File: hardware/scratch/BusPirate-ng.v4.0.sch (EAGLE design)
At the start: 133 parts, among them CON1 CON-USB-F-MICRO-B, IC10 74LVC1G07DBV, IC11 IC_BUFF_SN74LVC1T45DBV, IC12 74LVC1G07DBV, IC13 IC_BUFF_SN74LVC1T45DBV, IC14 74LVC1G07DBV, IC15 IC_BUFF_SN74LVC1T45DBV, IC16 74LVC1G07DBV, IC17 IC_BUFF_SN74LVC1T45DBV, IC2 IC_MEM_23LC1024, IC3 IC_MEM_23LC1024, IC4 IC_74AC573, IC5 IC_BL1551, IC6 IC_BL1551, IC7 74HCT4066PW, IC8 74LVC1G07DBV, IC9 IC_BUFF_SN74LVC1T45DBV, J1 CON_HEADER_1X04, J2 CON_HEADER_1X03-PTH, J3 CON_HEADER_2X02-PTH, J5 CON_HEADER_1X10-RIGHT_ANGLED_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, U1 IC_FPGA_ICE40HX4K, U2 IC_UC_STM32F103ZX, U3 IC_MEM_AT45DB041D

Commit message: connect remaining loose nets, finished routing -connect VCC of 74LVCT45 to pull-up voltage VPUN -connect pull-up resistors of FPGA_CRESET and FPGA_CDONE to to 3V3
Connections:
- removed net VCC: R38.2, R39.2
- removed net VCCEXT: C10.2, C2.2, C4.2, C6.2, C8.2, IC11.VCCB, IC13.VCCB, IC15.VCCB, IC17.VCCB, IC9.VCCB
- net 3V3: now also R38.2, R39.2
- net USBLED: no longer U2U.UART4_TX/USART3_TX('01')/FT/PC10
- net VPUN: now also C10.2, C2.2, C4.2, C6.2, C8.2, IC11.VCCB, IC13.VCCB, IC15.VCCB, IC17.VCCB, IC9.VCCB
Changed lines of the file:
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@@
 <attribute name="VALUE" x="76.2" y="375.92" size="1.778" layer="96"/>
 </instance>
-<instance part="P+1" gate="VCC" x="83.82" y="388.62"/>
-<instance part="P+3" gate="VCC" x="81.28" y="386.08"/>
+<instance part="P+1" gate="VCC" x="83.82" y="388.62" smashed="yes"/>
+<instance part="P+3" gate="VCC" x="81.28" y="388.62" smashed="yes"/>
 <instance part="C21" gate="G$1" x="-195.58" y="543.56" smashed="yes" rot="R180">
 <attribute name="NAME" x="-195.58" y="548.64" size="1.778" layer="95" rot="R90"/>
@@
 <junction x="144.78" y="284.48"/>
 </segment>
+<segment>
+<pinref part="R38" gate="G$1" pin="2"/>
+<pinref part="P+1" gate="VCC" pin="VCC"/>
+<wire x1="83.82" y1="386.08" x2="83.82" y2="383.54" width="0.1524" layer="91"/>
+<label x="83.82" y="388.62" size="1.778" layer="95"/>
+</segment>
+<segment>
+<pinref part="R39" gate="G$1" pin="2"/>
+<pinref part="P+3" gate="VCC" pin="VCC"/>
+<wire x1="81.28" y1="381" x2="81.28" y2="386.08" width="0.1524" layer="91"/>
+<label x="81.28" y="388.62" size="1.778" layer="95" align="bottom-right"/>
+</segment>
 </net>
 <net name="N$7" class="0">
@@
 <wire x1="-248.92" y1="139.7" x2="-251.46" y2="139.7" width="0.1524" layer="91"/>
 <label x="-251.46" y="139.7" size="1.778" layer="95" align="center-right"/>
-</segment>
-<segment>
-<pinref part="U2" gate="U" pin="UART4_TX/USART3_TX('01')/FT/PC10"/>
-<wire x1="-142.24" y1="121.92" x2="-139.7" y2="121.92" width="0.1524" layer="91"/>
 </segment>
 </net>
@@
 <pinref part="RN1" gate="C" pin="1"/>
 </segment>
+<segment>
+<pinref part="IC17" gate="G$1" pin="VCCB"/>
+<wire x1="175.26" y1="281.94" x2="175.26" y2="284.48" width="0.1524" layer="91"/>
+<label x="175.26" y="287.02" size="1.778" layer="95" align="center-right"/>
+<pinref part="C10" gate="G$1" pin="2"/>
+<wire x1="175.26" y1="284.48" x2="175.26" y2="287.02" width="0.1524" layer="91"/>
+<junction x="175.26" y="284.48"/>
+</segment>
+<segment>
+<pinref part="IC15" gate="G$1" pin="VCCB"/>
+<wire x1="179.07" y1="335.28" x2="179.07" y2="339.09" width="0.1524" layer="91"/>
+<label x="177.8" y="340.36" size="1.778" layer="95" align="center-right"/>
+<pinref part="C8" gate="G$1" pin="2"/>
+<wire x1="179.07" y1="339.09" x2="179.07" y2="341.63" width="0.1524" layer="91"/>
+<junction x="179.07" y="339.09"/>
+</segment>
+<segment>
+<pinref part="IC13" gate="G$1" pin="VCCB"/>
+<wire x1="175.26" y1="386.08" x2="175.26" y2="388.62" width="0.1524" layer="91"/>
+<label x="175.26" y="391.16" size="1.778" layer="95" align="center-right"/>
+<pinref part="C6" gate="G$1" pin="2"/>
+<wire x1="175.26" y1="388.62" x2="175.26" y2="391.16" width="0.1524" layer="91"/>
+<junction x="175.26" y="388.62"/>
+</segment>
+<segment>
+<pinref part="IC11" gate="G$1" pin="VCCB"/>
+<wire x1="175.26" y1="436.88" x2="175.26" y2="439.42" width="0.1524" layer="91"/>
+<label x="175.26" y="441.96" size="1.778" layer="95" align="center-right"/>
+<pinref part="C4" gate="G$1" pin="2"/>
+<wire x1="175.26" y1="439.42" x2="175.26" y2="441.96" width="0.1524" layer="91"/>
+<junction x="175.26" y="439.42"/>
+</segment>
+<segment>
+<pinref part="IC9" gate="G$1" pin="VCCB"/>
+<wire x1="175.26" y1="497.84" x2="175.26" y2="500.38" width="0.1524" layer="91"/>
+<label x="175.26" y="502.92" size="1.778" layer="95" align="center-right"/>
+<pinref part="C2" gate="G$1" pin="2"/>
+<wire x1="175.26" y1="500.38" x2="175.26" y2="502.92" width="0.1524" layer="91"/>
+<junction x="175.26" y="500.38"/>
+</segment>
 </net>
 <net name="UART_RX" class="0">
@@
 </segment>
 </net>
-<net name="VCC" class="0">
-<segment>
-<pinref part="R38" gate="G$1" pin="2"/>
-<pinref part="P+1" gate="VCC" pin="VCC"/>
-<wire x1="83.82" y1="386.08" x2="83.82" y2="383.54" width="0.1524" layer="91"/>
-</segment>
-<segment>
-<pinref part="R39" gate="G$1" pin="2"/>
-<pinref part="P+3" gate="VCC" pin="VCC"/>
-<wire x1="81.28" y1="381" x2="81.28" y2="383.54" width="0.1524" layer="91"/>
-</segment>
-</net>
-<net name="VCCEXT" class="0">
-<segment>
-<pinref part="IC9" gate="G$1" pin="VCCB"/>
-<wire x1="175.26" y1="497.84" x2="175.26" y2="500.38" width="0.1524" layer="91"/>
-<label x="175.26" y="502.92" size="1.778" layer="95" align="center-right"/>
-<pinref part="C2" gate="G$1" pin="2"/>
-<wire x1="175.26" y1="500.38" x2="175.26" y2="502.92" width="0.1524" layer="91"/>
-<junction x="175.26" y="500.38"/>
-</segment>
-<segment>
-<pinref part="IC11" gate="G$1" pin="VCCB"/>
-<wire x1="175.26" y1="436.88" x2="175.26" y2="439.42" width="0.1524" layer="91"/>
-<label x="175.26" y="441.96" size="1.778" layer="95" align="center-right"/>
-<pinref part="C4" gate="G$1" pin="2"/>
-<wire x1="175.26" y1="439.42" x2="175.26" y2="441.96" width="0.1524" layer="91"/>
-<junction x="175.26" y="439.42"/>
-</segment>
-<segment>
-<pinref part="IC13" gate="G$1" pin="VCCB"/>
-<wire x1="175.26" y1="386.08" x2="175.26" y2="388.62" width="0.1524" layer="91"/>
-<label x="175.26" y="391.16" size="1.778" layer="95" align="center-right"/>
-<pinref part="C6" gate="G$1" pin="2"/>
-<wire x1="175.26" y1="388.62" x2="175.26" y2="391.16" width="0.1524" layer="91"/>
-<junction x="175.26" y="388.62"/>
-</segment>
-<segment>
-<pinref part="IC15" gate="G$1" pin="VCCB"/>
-<wire x1="179.07" y1="335.28" x2="179.07" y2="339.09" width="0.1524" layer="91"/>
-<label x="177.8" y="340.36" size="1.778" layer="95" align="center-right"/>
-<pinref part="C8" gate="G$1" pin="2"/>
-<wire x1="179.07" y1="339.09" x2="179.07" y2="341.63" width="0.1524" layer="91"/>
-<junction x="179.07" y="339.09"/>
-</segment>
-<segment>
-<pinref part="IC17" gate="G$1" pin="VCCB"/>
-<wire x1="175.26" y1="281.94" x2="175.26" y2="284.48" width="0.1524" layer="91"/>
-<label x="175.26" y="287.02" size="1.778" layer="95" align="center-right"/>
-<pinref part="C10" gate="G$1" pin="2"/>
-<wire x1="175.26" y1="284.48" x2="175.26" y2="287.02" width="0.1524" layer="91"/>
-<junction x="175.26" y="284.48"/>
-</segment>
-</net>

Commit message: renumber parts
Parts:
- removed C55: 0.1uF, rcl:C-EUC0603
- removed IC17: IC_BUFF_SN74LVC1T45DBV, dp_devices.v6:IC_BUFF_SN74LVC1T45DBV
- removed R34, R35: 100K, rcl:R-EU_R0603
- removed R36: 1M, rcl:R-EU_R0603
- removed R37, R40: 10K, dp_devices:RESISTOR-0603
- removed R38: 10K, rcl:R-EU_R0603
- added C28: 0.1uF, rcl:C-EUC0603
- added IC1: IC_MEM_23LC1024, dp_devices:IC_MEM_23LC1024
- added R1: 1.5K, dp_devices.v6:RESISTOR-0603
- added R10, R11, R12, R9: 10K, resistor:R-EU_R0603
- added R21: 100K, rcl:R-EU_R0603
- C1: value 0.1uF -> 10uF; device rcl:C-EUC0603 -> rcl:CPOL-EUSMCA
- C10, C27: device rcl:C-EUC0603 -> dp_devices.v6:CAPACITOR_NPOL-0402
- C11: value 10uF -> 0.1uF; device rcl:CPOL-EUSMCA -> rcl:C-EUC0603
- C12, C32: value 1uf -> 0.1uF
- C13: value 1uF -> 0.1uF
- C16: value 1uF -> 22pF
- C17: value 0.1uF -> 1uF; device rcl:C-EUC0603 -> rcl:CPOL-EUSMCA
- C18: value 0.1uF -> 22pF
- C36: value 22pF -> 1uf
- C37: value 22pF -> 1uF
- C38: value 0.1uF -> 1uf
- C44: value 0.1uF -> 1uF
- C45, C47: device dp_devices.v6:CAPACITOR_NPOL-0402 -> rcl:C-EUC0603
- C53: value 1uF -> 0.1uF; device rcl:CPOL-EUSMCA -> rcl:C-EUC0603
- IC10, IC8: value 74LVC1G07DBV -> IC_BUFF_SN74LVC1T45DBV; device 74xx-little-de:74LVC1G07DBV -> dp_devices.v6:IC_BUFF_SN74LVC1T45DBV
- IC14: value 74LVC1G07DBV -> IC_BL1551; device 74xx-little-de:74LVC1G07DBV -> dp_devices.v6:IC_BL1551
- IC15: value IC_BUFF_SN74LVC1T45DBV -> IC_BL1551; device dp_devices.v6:IC_BUFF_SN74LVC1T45DBV -> dp_devices.v6:IC_BL1551
- IC16: value 74LVC1G07DBV -> 74HCT4066PW; device 74xx-little-de:74LVC1G07DBV -> 40xx:4066TS
- IC3: value IC_MEM_23LC1024 -> IC_74AC573; device dp_devices:IC_MEM_23LC1024 -> dp_devices:IC_74AC573-TSSOP-20
- IC4: value IC_74AC573 -> 74LVC1G07DBV; device dp_devices:IC_74AC573-TSSOP-20 -> 74xx-little-de:74LVC1G07DBV
- IC5, IC6: value IC_BL1551 -> 74LVC1G07DBV; device dp_devices.v6:IC_BL1551 -> 74xx-little-de:74LVC1G07DBV
- IC7: value 74HCT4066PW -> 74LVC1G07DBV; device 40xx:4066TS -> 74xx-little-de:74LVC1G07DBV
- J1: value CON_HEADER_1X04 -> CON_HEADER_2X02-PTH; device dp_devices.v6:CON_HEADER_1X04 -> dp_devices:CON_HEADER_2X02-PTH
- J2: value CON_HEADER_1X03-PTH -> CON_HEADER_1X04; device dp_devices.v6:CON_HEADER_1X03-PTH -> dp_devices.v6:CON_HEADER_1X04
- J3: value CON_HEADER_2X02-PTH -> CON_HEADER_1X03-PTH; device dp_devices:CON_HEADER_2X02-PTH -> dp_devices.v6:CON_HEADER_1X03-PTH
- R13, R14: value 10K -> 1K1; device resistor:R-EU_R0603 -> dp_devices:RESISTOR-0603
- R16: value 1K1 -> 10K; device dp_devices:RESISTOR-0603 -> rcl:R-EU_R0603
- R18: value 10K -> 1K1; device dp_devices.v6:RESISTOR-0603 -> dp_devices:RESISTOR-0603
- R19, R20: value 1K1 -> 100K; device dp_devices:RESISTOR-0603 -> rcl:R-EU_R0603
- R2: value 1.5K -> 22R
- R25, R26, R31: value 100K -> 1M
- R3: value 10K -> 22R; device rcl:R-EU_R0603 -> dp_devices.v6:RESISTOR-0603
- R30, R33: value 1M -> 100K
- R4: device rcl:R-EU_R0603 -> dp_devices:RESISTOR-0603
- R5: value 22R -> 10K
- R6: value 22R -> 10K; device dp_devices.v6:RESISTOR-0603 -> dp_devices:RESISTOR-0603
- R7, R8: device resistor:R-EU_R0603 -> rcl:R-EU_R0603
- U1: value IC_FPGA_ICE40HX4K -> IC_MEM_AT45DB041D; device dp_devices.v6:IC_FPGA_ICE40HX4K -> dp_devices.v6:IC_MEM_AT45DB041D
- U3: value IC_MEM_AT45DB041D -> IC_FPGA_ICE40HX4K; device dp_devices.v6:IC_MEM_AT45DB041D -> dp_devices.v6:IC_FPGA_ICE40HX4K
- VR3: value MCP1801T-5002I/OT -> MCP1801T-1202I/OT
- VR4: value MCP1801T-1202I/OT -> MCP1801T-5002I/OT
- renumbered J5 to J4, R39 to R15, XTAL2 to XTAL1
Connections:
- net 1V2: now also C23.2, C26.2, C27.1, C31.2, C35.2, C38.1, U3BANK0.VCC@0, U3BANK0.VCCPLL1, U3BANK1.VCC@0, U3BANK2.VCC@0, U3BANK2.VCCPLL0, U3BANK3.VCC@0, VR3.OUT; no longer C20.1, C32.1, C38.2, C41.2, C48.2, C55.2, U1BANK0.VCC@0, U1BANK0.VCCPLL1, U1BANK1.VCC@0, U1BANK2.VCC@0, U1BANK2.VCCPLL0, U1BANK3.VCC@0, VR4.OUT
- net 3V3: now also C10.1, C11.2, C12.2, C13.2, C15.2, C17.+, C19.2, C2.2, C20.1, C28.2, C3.2, C32.2, C36.1, C39.1, C4.2, C40.1, C41.1, C42.1, C43.1, C5.2, C50.1, C52.1, C54.1, C6.2, C7.2, C8.2, C9.2, IC10.VCCA, IC1SUP.V+, IC3IC.LE, IC3PWR.V+, IC4P.VCC, IC5P.VCC, IC6P.VCC, IC7P.VCC, IC8.VCCA, J1.2, J1.4, J2.1, R13.2, R19.2, R20.2, R21.2, R23.2, R5.2, U1.!RST, U1.!WP, U1.VCC, U3BANK0.VCCIO_0@0, U3BANK0.VCCIO_0@1, U3BANK1.VCCIO_1@0, U3BANK1.VCCIO_1@1, U3BANK1.VPP_2V5, U3BANK2.VCCIO_2@0, U3BANK2.VCCIO_2@1, U3BANK3.VCCIO_3@0, U3BANK3.VCCIO_3@1, U3SPI.VCC_SPI; no longer C1.1, C12.1, C14.1, C15.1, C17.1, C23.2, C26.2, C27.2, C3.1, C31.2, C35.2, C39.2, C40.2, C42.2, C43.2, C44.2, C45.1, C46.2, C47.1, C49.2, C5.1, C50.2, C52.2, C53.+, C54.2, C7.1, C9.1, IC10P.VCC, IC14P.VCC, IC15.VCCA, IC16P.VCC, IC17.VCCA, IC3SUP.V+, IC4IC.LE, IC4PWR.V+, IC8P.VCC, J1.1, J3.2, J3.4, R18.2, R25.2, R28.2, R31.2, R34.2, R38.2, U1BANK0.VCCIO_0@0, U1BANK0.VCCIO_0@1, U1BANK1.VCCIO_1@0, U1BANK1.VCCIO_1@1, U1BANK1.VPP_2V5, U1BANK2.VCCIO_2@0, U1BANK2.VCCIO_2@1, U1BANK3.VCCIO_3@0, U1BANK3.VCCIO_3@1, U1SPI.VCC_SPI, U3.!RST, U3.!WP, U3.VCC
- net ADC1: now also R10.2, R9.2; no longer R7.2, R8.2
- net ADC2: now also RN2A.2, RN2B.2; no longer RN1A.2, RN1B.2
- net ADC3: now also RN1C.2, RN1D.2; no longer RN2C.2, RN2D.2
- net ADC4: now also RN1A.2, RN1B.2; no longer RN2A.2, RN2B.2
- net ADC5: now also R11.2, R12.2; no longer R13.2, R14.2
- net ADC6: now also RN2C.2, RN2D.2; no longer RN1C.2, RN1D.2
- net BOOT0: now also J1.1, R8.1; no longer J3.1, R4.1
- net BOOT1: now also J1.3, R7.1; no longer J3.3, R3.1
- net BPIO_AUX: now also IC11.B, IC3IC.6D, IC7A.O, R27.2; no longer IC16A.O, IC17.B, IC4IC.6D, R36.2
- net BPIO_CLOCK: now also IC3IC.3D, IC5A.O, IC9.B, R25.2; no longer IC10A.O, IC11.B, IC4IC.3D, R27.2
- net BPIO_CS: now also IC12A.O, IC13.B, IC3IC.5D, R31.2; no longer IC14A.O, IC15.B, IC4IC.5D, R33.2
- net BPIO_MISO: now also IC10.B, IC3IC.4D, IC6A.O, R26.2; no longer IC12A.O, IC13.B, IC4IC.4D, R30.2
- net BPIO_MOSI: now also IC3IC.2D, IC4A.O, IC8.B; no longer IC4IC.2D, IC8A.O, IC9.B
- net BUFDIR_AUX: now also IC11.DIR, R32.2, U3BANK1.IOR_164; no longer IC17.DIR, R35.2, U1BANK1.IOR_164
- net BUFDIR_CLOCK: now also IC9.DIR, R29.2, U3BANK1.IOR_111; no longer IC11.DIR, R26.2, U1BANK1.IOR_111
- net BUFDIR_CS: now also IC13.DIR, R33.2, U3BANK1.IOR_167; no longer IC15.DIR, R32.2, U1BANK1.IOR_167
- net BUFDIR_MISO: now also IC10.DIR, R30.2, U3BANK1.IOR_118; no longer IC13.DIR, R29.2, U1BANK1.IOR_118
- net BUFDIR_MOSI: now also IC8.DIR, R28.2, U3BANK1.IOR_115; no longer IC9.DIR, R23.2, U1BANK1.IOR_115
- net BUFIO_AUX: now also IC11.A, U3BANK1.IOR_161; no longer IC17.A, U1BANK1.IOR_161
- net BUFIO_CLOCK: now also IC9.A, U3BANK1.IOR_110; no longer IC11.A, U1BANK1.IOR_110
- net BUFIO_CS: now also IC13.A, U3BANK1.IOR_166; no longer IC15.A, U1BANK1.IOR_166
- net BUFIO_MISO: now also IC10.A, U3BANK1.IOR_117; no longer IC13.A, U1BANK1.IOR_117
- net BUFIO_MOSI: now also IC8.A, U3BANK1.IOR_114; no longer IC9.A, U1BANK1.IOR_114
- net BUFOD_AUX: now also IC7A.I, R22.1, U3BANK1.IOR_160; no longer IC16A.I, R34.1, U1BANK1.IOR_160
- net BUFOD_CLOCK: now also IC5A.I, R20.1, U3BANK1.IOR_109; no longer IC10A.I, R25.1, U1BANK1.IOR_109
- net BUFOD_CS: now also IC12A.I, R23.1, U3BANK1.IOR_165; no longer IC14A.I, R31.1, U1BANK1.IOR_165
- net BUFOD_MISO: now also IC6A.I, R21.1, U3BANK1.IOR_116; no longer IC12A.I, R28.1, U1BANK1.IOR_116
- net BUFOD_MOSI: now also IC4A.I, R19.1, U3BANK1.IOR_112; no longer IC8A.I, R22.1, U1BANK1.IOR_112
- net D+: now also R1.1, R3.2; no longer R2.1, R6.2
- net D-: now also R2.2; no longer R5.2
- net FLASH_MISO: now also U1.SO; no longer U3.SO
- net FLASH_MOSI: now also U1.SI; no longer U3.SI
- net FLASH_SCK: now also U1.SCK; no longer U3.SCK
- net FPGA_CDONE: now also U3BANK2.CDONE; no longer U1BANK2.CDONE
- net FPGA_CRESET: now also R16.1, U3BANK2.CRESET_B; no longer R38.1, U1BANK2.CRESET_B
- net FPGA_PROG_CLOCK: now also U3SPI.IOB_107/SCK; no longer U1SPI.IOB_107/SCK
- net FPGA_PROG_CS: now also R6.1, U3SPI.IOB_108/SS; no longer R37.1, U1SPI.IOB_108/SS
- net FPGA_PROG_MISO: now also U3SPI.IOB_105/SDO; no longer U1SPI.IOB_105/SDO
- net FPGA_PROG_MOSI: now also U3SPI.IOB_106/SDI; no longer U1SPI.IOB_106/SDI
- net FSMC_A0: now also U3BANK3.IOL_3A; no longer U1BANK3.IOL_3A
- net FSMC_A1: now also U3BANK3.IOL_3B; no longer U1BANK3.IOL_3B
- net FSMC_A2: now also U3BANK3.IOL_4A; no longer U1BANK3.IOL_4A
- net FSMC_A3: now also U3BANK3.IOL_4B; no longer U1BANK3.IOL_4B
- net FSMC_A4: now also U3BANK3.IOL_5A; no longer U1BANK3.IOL_5A
- net FSMC_A5: now also U3BANK3.IOL_5B; no longer U1BANK3.IOL_5B
- net FSMC_D0: now also U3BANK3.IOL_17B; no longer U1BANK3.IOL_17B
- net FSMC_D1: now also U3BANK3.IOL_17A; no longer U1BANK3.IOL_17A
- net FSMC_D10: now also U3BANK3.IOL_18B; no longer U1BANK3.IOL_18B
- net FSMC_D11: now also U3BANK3.IOL_23A; no longer U1BANK3.IOL_23A
- net FSMC_D12: now also U3BANK3.IOL_23B; no longer U1BANK3.IOL_23B
- net FSMC_D13: now also U3BANK3.IOL_25A; no longer U1BANK3.IOL_25A
- net FSMC_D14: now also U3BANK3.IOL_24B; no longer U1BANK3.IOL_24B
- net FSMC_D15: now also U3BANK3.IOL_24A; no longer U1BANK3.IOL_24A
- net FSMC_D2: now also U3BANK3.IOL_2A; no longer U1BANK3.IOL_2A
- net FSMC_D3: now also U3BANK3.IOL_2B; no longer U1BANK3.IOL_2B
- net FSMC_D4: now also U3BANK3.IOL_10A; no longer U1BANK3.IOL_10A
- net FSMC_D5: now also U3BANK3.IOL_10B; no longer U1BANK3.IOL_10B
- net FSMC_D6: now also U3BANK3.IOL_12A; no longer U1BANK3.IOL_12A
- net FSMC_D7: now also U3BANK3.IOL_12B; no longer U1BANK3.IOL_12B
- net FSMC_D8: now also U3BANK3.IOL_13A; no longer U1BANK3.IOL_13A
- net FSMC_D9: now also U3BANK3.IOL_18A; no longer U1BANK3.IOL_18A
- net FSMC_NE3_CE: now also U3BANK3.IOL_14B; no longer U1BANK3.IOL_14B
- net FSMC_NOE_OE: now also U3BANK3.IOL_8A; no longer U1BANK3.IOL_8A
- net FSMC_NWE_WE: now also U3BANK3.IOL_8B; no longer U1BANK3.IOL_8B
- net GND: now also C1.-, C10.2, C11.1, C12.1, C13.1, C14.1, C15.1, C16.1, C17.-, C18.1, C19.1, C27.2, C28.1, C3.1, C32.1, C36.2, C37.2, C38.2, C39.2, C40.2, C41.2, C42.2, C43.2, C44.2, C45.1, C47.1, C5.1, C50.2, C51.2, C52.2, C53.2, C54.2, C7.1, C9.1, IC10.GND, IC14.GND, IC16P.VSS, IC1SUP.GND, IC3IC.1D, IC3PWR.GND, IC4P.GND, IC5P.GND, IC6P.GND, IC7P.GND, IC8.GND, J2.2, J3.1, R10.1, R12.1, R25.1, R28.1, R31.1, R6.2, R7.2, R8.2, U1.!CS, U1.GND, U3BANK0.GND@0, U3BANK0.GND@1, U3BANK0.GNDPLL1, U3BANK1.GND@0, U3BANK1.GND@1, U3BANK2.GND@0, U3BANK2.GNDPLL0, U3BANK3.GND@0, U3BANK3.GND@1, U3BANK3.GND@2, U3SPI.GND@0; no longer C1.2, C10.1, C11.-, C12.2, C13.2, C14.2, C15.2, C16.2, C17.2, C18.2, C19.2, C27.1, C3.2, C32.2, C36.1, C37.1, C38.1, C39.1, C40.1, C41.1, C42.1, C43.1, C44.1, C45.2, C47.2, C5.2, C50.1, C51.1, C52.1, C53.-, C54.1, C55.1, C7.2, C9.2, IC10P.GND, IC14P.GND, IC16P.GND, IC17.GND, IC3SUP.GND, IC4IC.1D, IC4PWR.GND, IC5.GND, IC6.GND, IC7P.VSS, IC8P.GND, J1.2, J2.1, R14.1, R23.1, R3.2, R35.1, R36.1, R37.2, R40.2, R8.1, U1BANK0.GND@0, U1BANK0.GND@1, U1BANK0.GNDPLL1, U1BANK1.GND@0, U1BANK1.GND@1, U1BANK2.GND@0, U1BANK2.GNDPLL0, U1BANK3.GND@0, U1BANK3.GND@1, U1BANK3.GND@2, U1SPI.GND@0, U3.!CS, U3.GND
- net IO_ADC/DAC: now also R9.1; no longer R7.1
- net LAT_AUX0: now also IC3IC.6Q, U3BANK1.IOR_147; no longer IC4IC.6Q, U1BANK1.IOR_147
- net LAT_AUX1: now also IC3IC.1Q, U3BANK1.IOR_139; no longer IC4IC.1Q, U1BANK1.IOR_139
- net LAT_CLK: now also IC3IC.3Q, U3BANK1.GBIN2/IOR_141; no longer IC4IC.3Q, U1BANK1.GBIN2/IOR_141
- net LAT_CS: now also IC3IC.5Q, U3BANK1.IOR_146; no longer IC4IC.5Q, U1BANK1.IOR_146
- net LAT_MISO: now also IC3IC.4Q, U3BANK1.IOR_144; no longer IC4IC.4Q, U1BANK1.IOR_144
- net LAT_MOSI: now also IC3IC.2Q, U3BANK1.GBIN3/IOR_140; no longer IC4IC.2Q, U1BANK1.GBIN3/IOR_140
- net LAT_OE: now also IC3IC.!OE, U3BANK1.IOR_138; no longer IC4IC.!OE, U1BANK1.IOR_138
- net LAT_SWV33: now also IC3IC.7Q, U3BANK1.IOR_148; no longer IC4IC.7Q, U1BANK1.IOR_148
- net LAT_SWV50: now also IC3IC.8Q, U3BANK1.IOR_152; no longer IC4IC.8Q, U1BANK1.IOR_152
- net LD1: now also R14.2; no longer R17.2
- net MCU_INT0: now also U3BANK0.GBIN0/IOT_198; no longer U1BANK0.GBIN0/IOT_198
- net MCU_INT1: now also U3BANK0.GBIN1/IOT_197; no longer U1BANK0.GBIN1/IOT_197
- net MCU_MCO: now also U3BANK3.GBIN7/IOL_13B; no longer U1BANK3.GBIN7/IOL_13B
- net MS0: now also SW2.1, SW2.2; no longer SW1.1, SW1.2
- net N$1: now also IC14.B, IC15.A1; no longer IC5.B, IC6.A1
- net N$11: now also U3BANK0.IOT_192; no longer U1BANK0.IOT_192
- net N$12: now also U3BANK0.IOT_191; no longer U1BANK0.IOT_191
- net N$13: now also R18.1; no longer R20.1
- net N$14: now also U3BANK0.IOT_190; no longer U1BANK0.IOT_190
- net N$16: now also U3BANK0.IOT_181; no longer U1BANK0.IOT_181
- net N$17: now also U3BANK3.IOL_25B; no longer U1BANK3.IOL_25B
- net N$18: now also R17.1; no longer R19.1
- net N$2: now also IC16A.A; no longer IC7A.A
- net N$20: now also U3BANK0.IOT_179; no longer U1BANK0.IOT_179
- net N$24: now also U3BANK0.IOT_168; no longer U1BANK0.IOT_168
- net N$26: now also U3BANK0.IOT_178; no longer U1BANK0.IOT_178
- net N$3: now also IC16B.A; no longer IC7B.A
- net N$4: now also IC16C.A; no longer IC7C.A
- net N$48: now also U3BANK0.IOT_174; no longer U1BANK0.IOT_174
- net N$49: now also U3BANK0.IOT_177; no longer U1BANK0.IOT_177
- net N$5: now also IC16D.A; no longer IC7D.A
- net N$6: now also R14.1; no longer R17.1
- net N$7: now also R13.1; no longer R16.1
- net N$8: now also C18.2; no longer C37.2
- net N$9: now also C16.2; no longer C36.2
- net PWM: now also U3BANK3.GBIN6/IOL_14A; no longer U1BANK3.GBIN6/IOL_14A
- net RST: now also C14.2, R5.1, SW1.1, SW1.2; no longer C51.2, R18.1, SW2.1, SW2.2
- net SRAM0_CS: now also IC1IC.!CS, U3BANK0.IOT_222; no longer IC2IC.!CS, U1BANK0.IOT_222
- net SRAM0_SIO0: now also IC1IC.SI/SIO0, U3BANK0.IOT_216; no longer IC2IC.SI/SIO0, U1BANK0.IOT_216
- net SRAM0_SIO1: now also IC1IC.SO/SIO1, U3BANK0.IOT_220; no longer IC2IC.SO/SIO1, U1BANK0.IOT_220
- net SRAM0_SIO2: now also IC1IC.SIO2, U3BANK0.IOT_217; no longer IC2IC.SIO2, U1BANK0.IOT_217
- net SRAM0_SIO3: now also IC1IC.!HOLD/SIO3, U3BANK0.IOT_221; no longer IC2IC.!HOLD/SIO3, U1BANK0.IOT_221
- net SRAM1_CS: now also IC2IC.!CS, U3BANK0.IOT_173; no longer IC3IC.!CS, U1BANK0.IOT_173
- net SRAM1_SIO0: now also IC2IC.SI/SIO0, U3BANK0.IOT_169; no longer IC3IC.SI/SIO0, U1BANK0.IOT_169
- net SRAM1_SIO1: now also IC2IC.SO/SIO1, U3BANK0.IOT_171; no longer IC3IC.SO/SIO1, U1BANK0.IOT_171
- net SRAM1_SIO2: now also IC2IC.SIO2, U3BANK0.IOT_170; no longer IC3IC.SIO2, U1BANK0.IOT_170
- net SRAM1_SIO3: now also IC2IC.!HOLD/SIO3, U3BANK0.IOT_172; no longer IC3IC.!HOLD/SIO3, U1BANK0.IOT_172
- net SRAM_CLOCK: now also IC1IC.SCK, U3BANK0.IOT_219; no longer IC3IC.SCK, U1BANK0.IOT_219
- net SWCLK: now also J2.4; no longer J1.4
- net SWDIO: now also J2.3; no longer J1.3
- net SWV33: now also C37.1, IC14.A2, IC3IC.7D, RN1C.1; no longer C13.1, IC4IC.7D, IC5.A2, RN2C.1
- net SWV50: now also C44.1, IC14.A1, IC3IC.8D, RN1B.1, VR4.OUT; no longer C16.1, IC4IC.8D, IC5.A1, RN2B.1, VR3.OUT
- net UART_RX: now also J3.2; no longer J2.2
- net UART_TX: now also J3.3; no longer J2.3
- net USBLED: now also R18.2; no longer R20.2
- net USB_D+: now also R3.1; no longer R6.1
- net USB_D-: now also R2.1; no longer R5.1
- net USB_DET: now also R1.2; no longer R2.2
- net V33PU: now also IC15.ENB; no longer IC6.ENB
- net V50PU: now also IC14.ENB; no longer IC5.ENB
- net VEXTERN: now also IC15.A2, RN2B.1; no longer IC6.A2, RN1B.1
- net VEXTPU: now also IC16A.C, IC16B.C, IC16C.C, IC16D.C; no longer IC7A.C, IC7B.C, IC7C.C, IC7D.C
- net VPUN: now also C45.2, C46.2, C47.2, C48.2, C49.2, IC10.VCCB, IC15.B, IC16A.B, IC16B.B, IC16C.B, IC16D.B, IC8.VCCB, RN2C.1; no longer C10.2, C2.2, C4.2, C6.2, C8.2, IC15.VCCB, IC17.VCCB, IC6.B, IC7A.B, IC7B.B, IC7C.B, IC7D.B, RN1C.1
- net VREGEN: now also R17.2, R4.1, VR4.EN; no longer R19.2, R40.1, VR3.EN
- net VUSB: now also C1.+, C51.1, C53.1, IC14.VCC, IC15.VCC, IC16P.VDD, R11.1, VR3.EN; no longer C11.+, C18.1, C19.1, IC5.VCC, IC6.VCC, IC7P.VDD, R13.1, VR4.EN
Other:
- moved on the sheet: C12, C13, C14, C15, C16, C18, C19, C2, C20, C21, C22, C23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

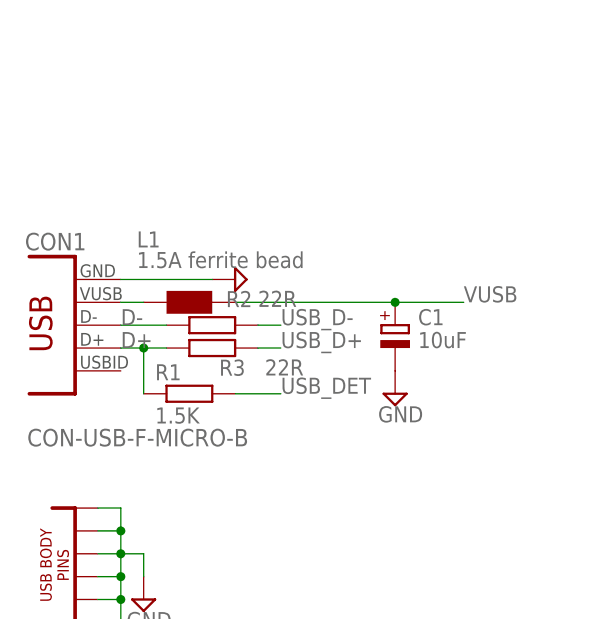
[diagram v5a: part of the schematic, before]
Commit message: replaced USB mini-B connector, fix DRC errors on the said connector
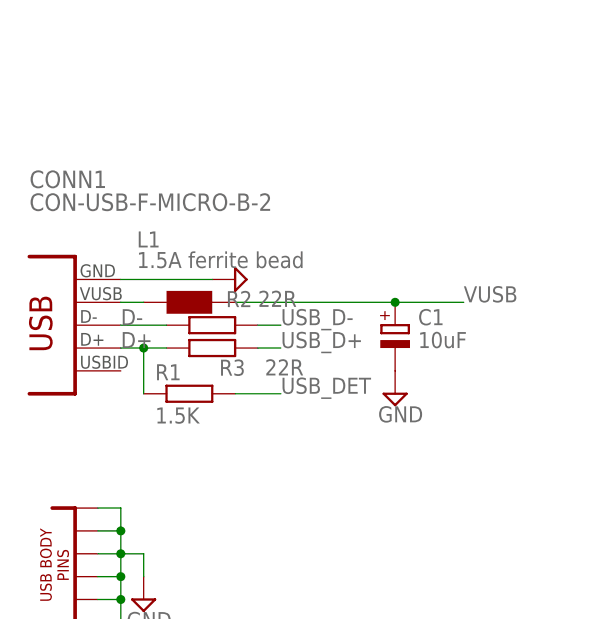
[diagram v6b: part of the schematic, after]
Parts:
- removed CON1: CON-USB-F-MICRO-B, dp_devices.v6:CON-USB-F-MICRO-B
- added CONN1: CON-USB-F-MICRO-B-2, dp_devices.v6:CON-USB-F-MICRO-B-2
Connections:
- net D+: now also CONN1CON.D+; no longer CON1CON1.D+
- net D-: now also CONN1CON.D-; no longer CON1CON1.D-
- net EXVUSB: now also CONN1CON.VUSB; no longer CON1CON1.VUSB
- net GND: now also CONN1BGND.P$1, CONN1BGND.P$2, CONN1BGND.P$3, CONN1BGND.P$4, CONN1BGND.P$5, CONN1BGND.P$6, CONN1CON.GND; no longer CON1CON1.GND, CON1GPINS.P$1, CON1GPINS.P$2, CON1GPINS.P$3, CON1GPINS.P$4, CON1GPINS.P$5, CON1GPINS.P$6
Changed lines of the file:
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@@
 <part name="SUPPLY98" library="supply2" deviceset="GND" device=""/>
 <part name="SUPPLY99" library="supply2" deviceset="GND" device=""/>
-<part name="CON1" library="dp_devices.v6" deviceset="CON-USB-F-MICRO-B" device=""/>
 <part name="SUPPLY74" library="supply2" deviceset="GND" device=""/>
 <part name="SUPPLY51" library="supply2" deviceset="GND" device=""/>
@@
 <part name="C20" library="dp_devices.v6" deviceset="CAPACITOR_NPOL" device="-0402" value="0.1uF"/>
 <part name="C10" library="dp_devices.v6" deviceset="CAPACITOR_NPOL" device="-0402" value="0.1uF"/>
+<part name="CONN1" library="dp_devices.v6" deviceset="CON-USB-F-MICRO-B-2" device=""/>
 </parts>
 <sheets>
@@
 <instance part="SUPPLY98" gate="GND" x="213.36" y="157.48"/>
 <instance part="SUPPLY99" gate="GND" x="243.84" y="175.26"/>
-<instance part="CON1" gate="CON1" x="-350.52" y="480.06" smashed="yes">
-<attribute name="NAME" x="-356.108" y="488.3785" size="1.9304" layer="95"/>
-<attribute name="VALUE" x="-355.854" y="466.598" size="1.9304" layer="96"/>
-</instance>
-<instance part="CON1" gate="GPINS" x="-350.52" y="452.12"/>
 <instance part="SUPPLY74" gate="GND" x="149.86" y="551.18" smashed="yes" rot="MR270"/>
 <instance part="SUPPLY51" gate="GND" x="50.8" y="71.12" smashed="yes" rot="MR270"/>
@@
 <attribute name="VALUE" x="-160.02" y="556.26" size="1.778" layer="96" rot="R90"/>
 </instance>
+<instance part="CONN1" gate="CON" x="-350.52" y="480.06" smashed="yes">
+<attribute name="NAME" x="-355.6" y="495.3" size="1.9304" layer="95"/>
+<attribute name="VALUE" x="-355.6" y="492.76" size="1.9304" layer="96"/>
+</instance>
+<instance part="CONN1" gate="BGND" x="-350.52" y="452.12"/>
 </instances>
 <busses>
@@
 <pinref part="SUPPLY2" gate="GND" pin="GND"/>
 <wire x1="-335.28" y1="485.14" x2="-345.44" y2="485.14" width="0.1524" layer="91"/>
-<pinref part="CON1" gate="CON1" pin="GND"/>
+<pinref part="CONN1" gate="CON" pin="GND"/>
 </segment>
 <segment>
@@
 </segment>
 <segment>
-<pinref part="CON1" gate="GPINS" pin="P$6"/>
 <wire x1="-347.98" y1="447.04" x2="-345.44" y2="447.04" width="0.1524" layer="91"/>
 <wire x1="-345.44" y1="447.04" x2="-345.44" y2="449.58" width="0.1524" layer="91"/>
-<pinref part="CON1" gate="GPINS" pin="P$1"/>
 <wire x1="-345.44" y1="449.58" x2="-345.44" y2="452.12" width="0.1524" layer="91"/>
 <wire x1="-345.44" y1="452.12" x2="-345.44" y2="454.66" width="0.1524" layer="91"/>
@@
 <wire x1="-345.44" y1="457.2" x2="-345.44" y2="459.74" width="0.1524" layer="91"/>
 <wire x1="-347.98" y1="459.74" x2="-345.44" y2="459.74" width="0.1524" layer="91"/>
-<pinref part="CON1" gate="GPINS" pin="P$2"/>
 <wire x1="-347.98" y1="457.2" x2="-345.44" y2="457.2" width="0.1524" layer="91"/>
-<pinref part="CON1" gate="GPINS" pin="P$3"/>
 <wire x1="-347.98" y1="454.66" x2="-345.44" y2="454.66" width="0.1524" layer="91"/>
-<pinref part="CON1" gate="GPINS" pin="P$4"/>
 <wire x1="-347.98" y1="452.12" x2="-345.44" y2="452.12" width="0.1524" layer="91"/>
-<pinref part="CON1" gate="GPINS" pin="P$5"/>
 <wire x1="-347.98" y1="449.58" x2="-345.44" y2="449.58" width="0.1524" layer="91"/>
 <pinref part="SUPPLY1" gate="GND" pin="GND"/>
@@
 <junction x="-345.44" y="452.12"/>
 <junction x="-345.44" y="449.58"/>
+<pinref part="CONN1" gate="BGND" pin="P$1"/>
+<pinref part="CONN1" gate="BGND" pin="P$2"/>
+<pinref part="CONN1" gate="BGND" pin="P$3"/>
+<pinref part="CONN1" gate="BGND" pin="P$4"/>
+<pinref part="CONN1" gate="BGND" pin="P$5"/>
+<pinref part="CONN1" gate="BGND" pin="P$6"/>
 </segment>
 <segment>
@@
 <pinref part="L1" gate="G$1" pin="1"/>
 <wire x1="-342.9" y1="482.6" x2="-345.44" y2="482.6" width="0.1524" layer="91"/>
-<pinref part="CON1" gate="CON1" pin="VUSB"/>
+<pinref part="CONN1" gate="CON" pin="VUSB"/>
 </segment>
 </net>
@@
 <pinref part="R1" gate="R" pin="1"/>
 <wire x1="-342.9" y1="477.52" x2="-345.44" y2="477.52" width="0.1524" layer="91"/>
-<pinref part="CON1" gate="CON1" pin="D+"/>
 <pinref part="R3" gate="R" pin="2"/>
+<pinref part="CONN1" gate="CON" pin="D+"/>
 </segment>
 </net>
@@
 <label x="-345.44" y="480.06" size="1.778" layer="95"/>
 <wire x1="-340.36" y1="480.06" x2="-345.44" y2="480.06" width="0.1524" layer="91"/>
-<pinref part="CON1" gate="CON1" pin="D-"/>
 <pinref part="R2" gate="R" pin="2"/>
-</segment>
-</net>
+<pinref part="CONN1" gate="CON" pin="D-"/>
+</segment>
+</net>

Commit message: Auxillary connection from MCU to FPGA -MCU_AUX1 FPGA_137 -> PC10 -MCU_AUX2 FPGA_136 -> PC11 -MCU_AUX3 FPGA_135 -> PC12 -MCU_AUX4 FPGA_134 -> PD6 -MCU_AUX5 FPGA_125 -> PB8 -MCU_AUX6 FPGA_124 -> PB9 -MCU_AUX7 FPGA_119 -> PE0 -MCU_AUX8 FPGA_118 -> PE1
gave SRAM each FPGA clock pins, SRAM0_CLOCK and SRAM1_CLOCK
-moved around SRAM1's pins of FPGA
-SRAM1_CS from FPGA_116 to FPGA_117
-SRAM1_SIO3 from FPGA_115 to FPGA_116
-SRAM_SIO1 from FPGA_114 to FPGA_115
-new FPGA pin SRAM1_CLOCK to FPGA_114
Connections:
- removed net N$11: U3BANK0.IOT_192
- removed net N$12: U3BANK0.IOT_191
- removed net N$26: U3BANK0.IOT_178
- removed net N$32: U2U.TIM4_CH3('0')/I2C1_SCL('1')/FT/PB8
- removed net N$33: U2U.TIM4_CH4('0')/I2C1_SDA('1')/FT/PB9
- removed net N$48: U3BANK0.IOT_174
- removed net N$49: U3BANK0.IOT_177
- removed net SRAM_CLOCK: IC1IC.SCK, IC2IC.SCK, U3BANK0.IOT_219
- new net MCU_AUX1: U2U.UART4_TX/USART3_TX('01')/FT/PC10, U3BANK0.IOT_215
- new net MCU_AUX2: U2U.UART4_RX/USART3_RX('01')/FT/PC11, U3BANK0.IOT_214
- new net MCU_AUX3: U2U.UART5_TX/USART3_CK('01')/FT/PC12, U3BANK0.IOT_213
- new net MCU_AUX4: U2U.PD6/FT/FSMC_NWAIT/USART2_RX('1'), U3BANK0.IOT_212
- new net MCU_AUX5: U2U.TIM4_CH3('0')/I2C1_SCL('1')/FT/PB8, U3BANK0.IOT_192
- new net MCU_AUX6: U2U.TIM4_CH4('0')/I2C1_SDA('1')/FT/PB9, U3BANK0.IOT_191
- new net MCU_AUX7: U2U.PE0/FT/TIM4_ETR/FSMC_NBL0, U3BANK0.IOT_178
- new net MCU_AUX8: U2U.PE1/FT/FSMC_NBL1, U3BANK0.IOT_177
- new net N$21: U3BANK0.IOT_206
- new net N$56: U2U.PD7/FT/FSMC_NE1/FSMC_NCE2/USART2_CK('1')
- new net N$57: U2U.PG11/FT/FSMC_NCE4_2
- new net N$58: U2U.PG12/FT/FSMC_NE4
- new net N$59: U2U.PG13/FT/FSMC_A24
- new net N$60: U2U.PG14/FT/FSMC_A25
- new net N$61: U2U.PG15/FT
- new net SRAM0_CLOCK: IC1IC.SCK, U3BANK0.IOT_219
- new net SRAM1_CLOCK: IC2IC.SCK, U3BANK0.IOT_171
- net SRAM1_CS: now also U3BANK0.IOT_174; no longer U3BANK0.IOT_173
- net SRAM1_SIO1: now also U3BANK0.IOT_172; no longer U3BANK0.IOT_171
- net SRAM1_SIO3: now also U3BANK0.IOT_173; no longer U3BANK0.IOT_172
